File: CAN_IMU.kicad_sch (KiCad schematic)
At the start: 36 parts, among them J1 USB_C_Receptacle_USB2.0_16P, J2 TAG SWD, J3 Conn_01x05, SW1 RST, SW2 SW_DIP_x02, U1 STM32G431CBTx, U2 USBLC6-2SC6, U3 SN74LVC1G126DBV, U4 TCAN3414, U5 TPS62172DSG

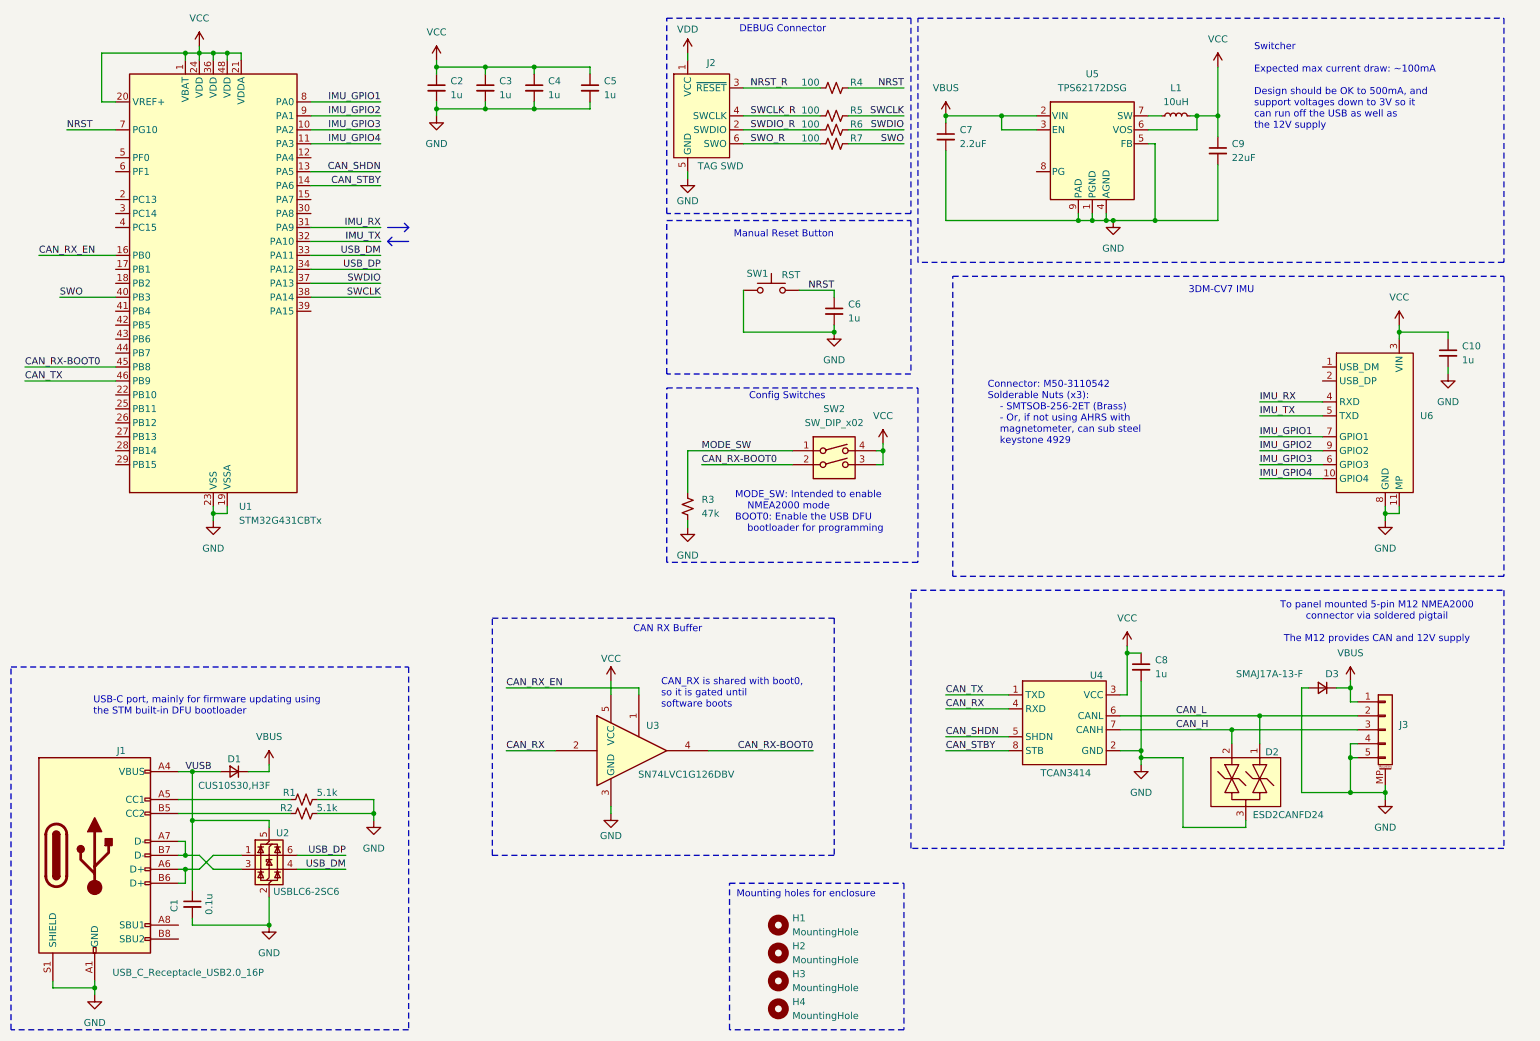
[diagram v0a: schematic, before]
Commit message: Add pulldown to CAN_RX_EN
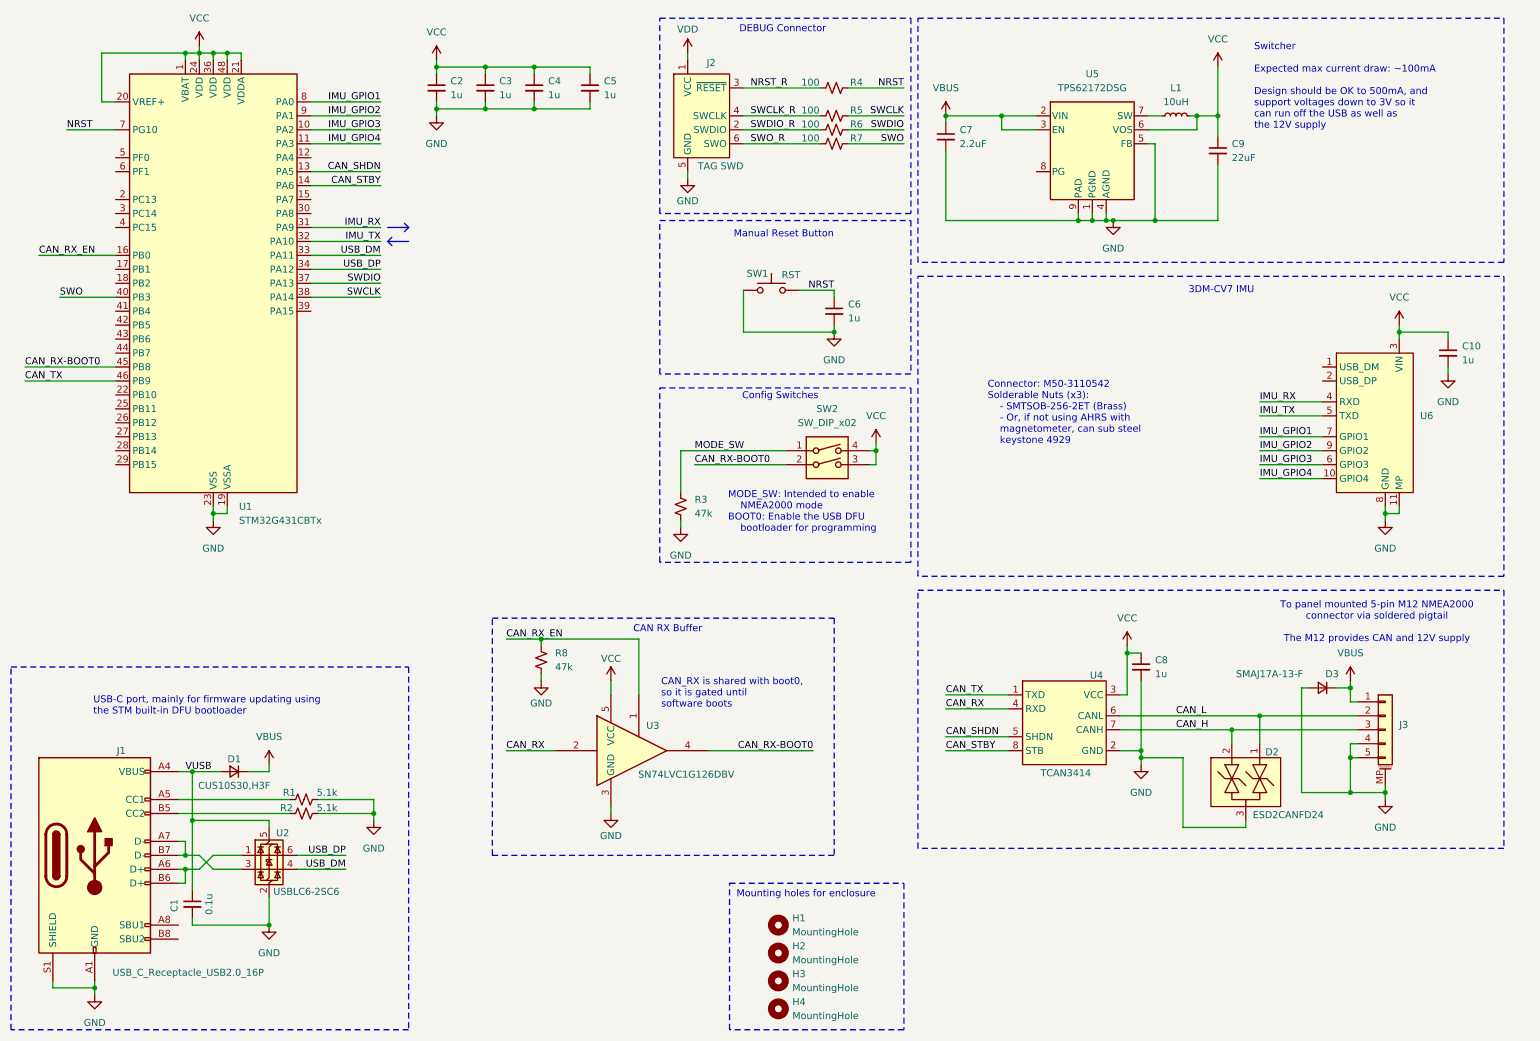
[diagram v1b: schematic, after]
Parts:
- added R8: 47k, Resistor_SMD:R_0603_1608Metric, symbol Device:R_Small_US
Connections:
- net CAN_RX_EN: now also R8.1
- net GND: now also R8.2
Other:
- moved on the sheet: R3, SW2

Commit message: Basically finished layout
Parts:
- C7: value 2.2uF -> 10uF; Digikey Part Number 1276-6702-1-ND -> 490-18663-1-ND; Mfg Part Number CL21A225KBFNNNE -> GRM21BR61H106KE43L
- L1: value 10uH -> 2.2uH; footprint Inductor_SMD:L_Bourns-SRN6028 -> RJMP_Inductors:IND_LQH5BPN2R2NT0L; Digikey Part Number 118-SRN6028C-100MCT-ND -> 490-7778-1-ND; Mfg Part Number SRN6028C-100M -> LQH5BPN2R2NT0L
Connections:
- net VDD is gone; now on net VCC: J2.1 (VCC)
- net CAN_H: now also D2.1; no longer D2.2
- net CAN_L: now also D2.2; no longer D2.1
- net CAN_RX_EN: now also U1.44 (PB7); no longer U1.16 (PB0)
- net CAN_SHDN: now also U1.41 (PB4); no longer U1.13 (PA5)
- net CAN_STBY: now also U1.43 (PB6); no longer U1.14 (PA6)
- net GND: no longer U6.11 (MP)
- net IMU_GPIO1: now also U1.28 (PB14); no longer U1.8 (PA0)
- net IMU_GPIO2: now also U1.27 (PB13); no longer U1.9 (PA1)
- net IMU_GPIO3: now also U1.25 (PB11); no longer U1.10 (PA2)
- net IMU_GPIO4: now also U1.26 (PB12); no longer U1.11 (PA3)
- net MODE_SW: now also U1.12 (PA4)
- net SW: now reaches L1.1, U5.7 (SW)
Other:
- moved on the sheet: L1

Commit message: Add part numbers and output generation
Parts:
- C10, C2, C3, C4, C5, C6, C8: LCSC Part Number (none) -> C15849
- C7: LCSC Part Number (none) -> C15850
- C9: Digikey Part Number (none) -> 1276-3047-1-ND; LCSC Part Number (none) -> C12891; Mfg Part Number (none) -> CL31A226KAHNNNE
- D1: LCSC Part Number (none) -> C146335
- D2: LCSC Part Number (none) -> C5278878
- D3: LCSC Part Number (none) -> C134963
- H1, H2, H3, H4, J2: now not fitted
- J1: LCSC Part Number (none) -> C2896636
- J3: LCSC Part Number (none) -> C265085
- L1: LCSC Part Number (none) -> C135262
- R3, R8: Digikey Part Number (none) -> 311-47.0KHRCT-ND; LCSC Part Number (none) -> C25819; Mfg Part Number (none) -> RC0603FR-0747KL
- R4, R5, R6, R7: LCSC Part Number (none) -> C105588
- SW2: LCSC Part Number (none) -> C3312524
- U1: Digikey Part Number (none) -> 497-19473-ND; LCSC Part Number (none) -> C529355; Mfg Part Number (none) -> STM32G431CBT6
- U3: LCSC Part Number (none) -> C46472327
- U4: LCSC Part Number (none) -> C22396693
- U5: Digikey Part Number (none) -> 296-39449-1-ND; LCSC Part Number (none) -> C59873; Mfg Part Number (none) -> TPS62172DSGR
- U6: Digikey Part Number (none) -> 952-2342-ND; LCSC Part Number (none) -> C6659241; Mfg Part Number (none) -> M50-3110542

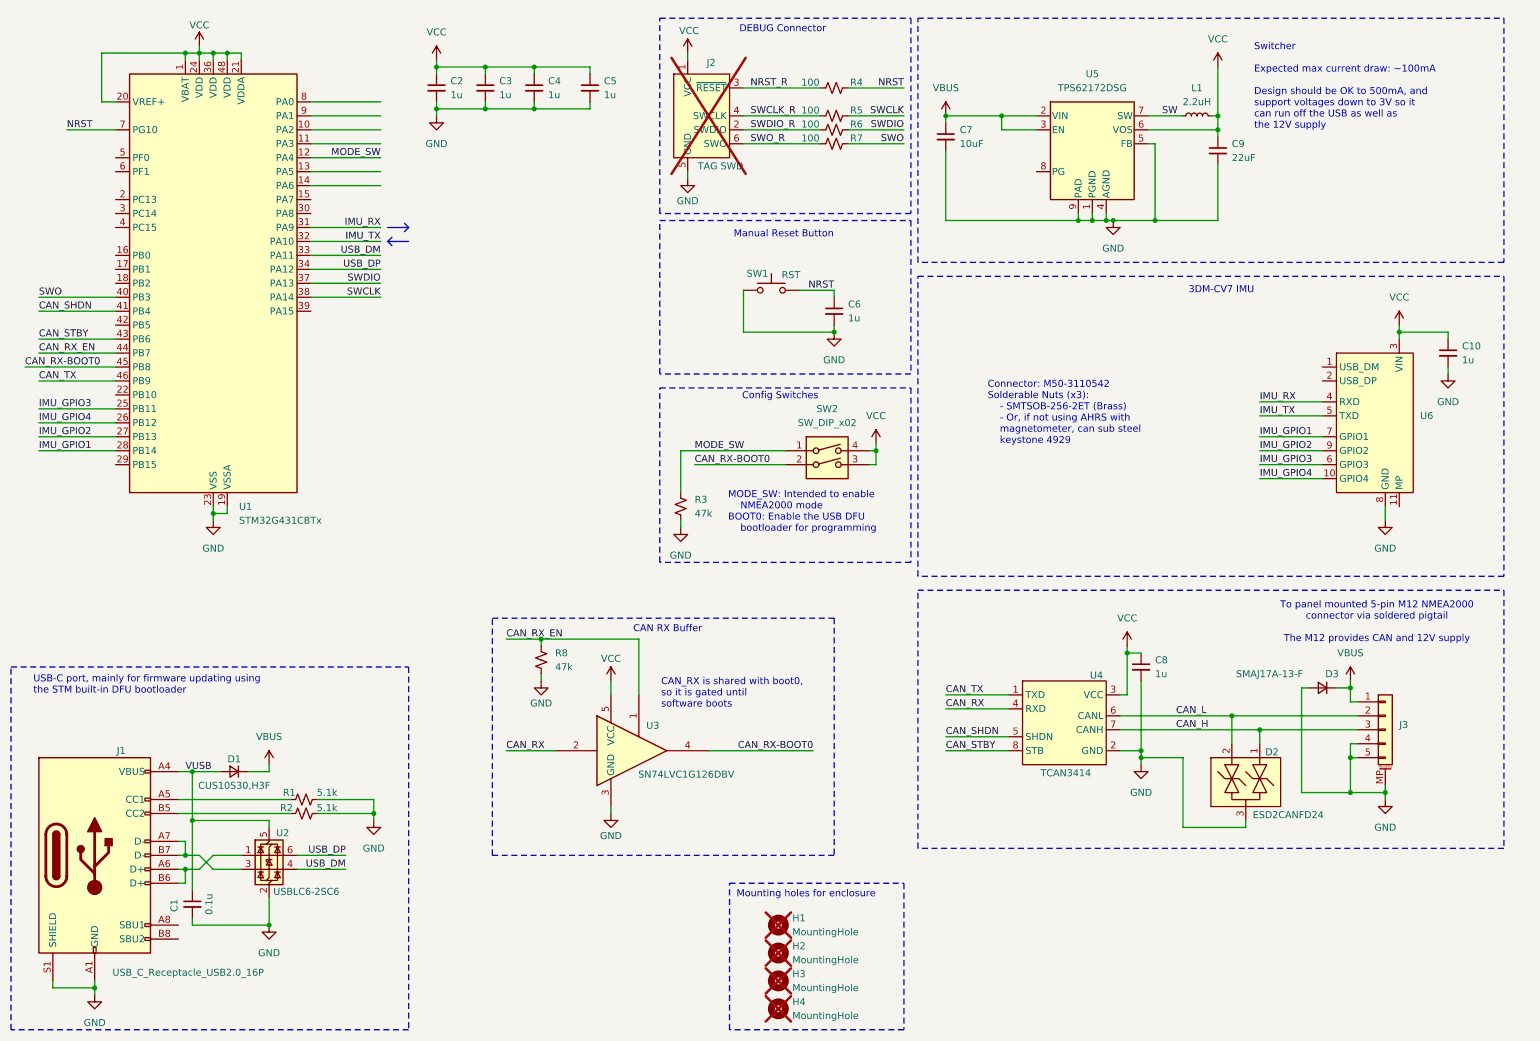
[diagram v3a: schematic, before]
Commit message: Add onboard IMU and logo
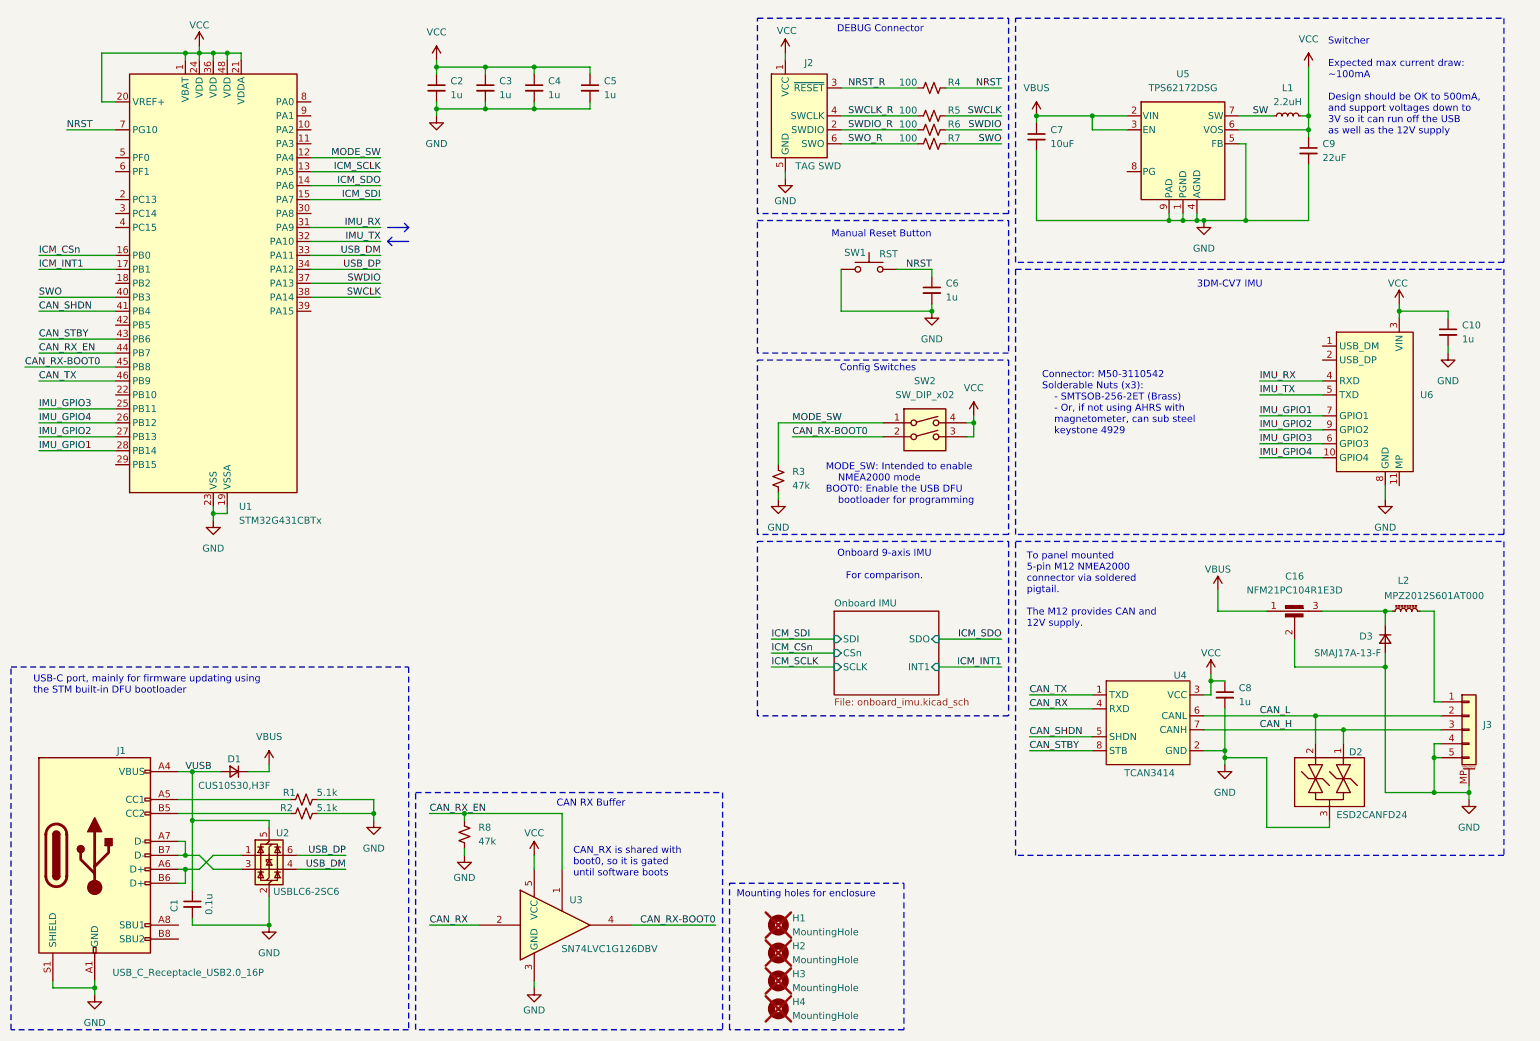
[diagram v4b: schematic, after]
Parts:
- added C16: NFM21PC104R1E3D, RJMP_Misc:NFM21PC_Feedthrough_Cap, symbol Device:C_Feedthrough
- added L2: MPZ2012S601AT000, Inductor_SMD:L_0805_2012Metric, symbol Device:L_Ferrite_Small
- J2: now fitted
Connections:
- net GND: now also C16.2
- net VBUS: now also C16.1; no longer D3.1 (K), J3.1 (Pin_1)
- net ICM_SCLK: now reaches U1.13 (PA5)
- net ICM_SDO: now reaches U1.14 (PA6)
- net ICM_SDI: now reaches U1.15 (PA7)
- net ICM_CSn: now reaches U1.16 (PB0)
- net ICM_INT1: now reaches U1.17 (PB1)
- new net: C16.3, D3.1 (K), L2.1
- new net: J3.1 (Pin_1), L2.2
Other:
- added sheet Onboard IMU (onboard_imu.kicad_sch)
- note added: "Onboard 9-axis IMU For comparison."
- note added: "To panel mounted 5-pin M12 NMEA2000 connector via soldered pigtail. The M12 provides CAN and 12V supply."
- note removed: "To panel mounted 5-pin M12 NMEA2000 connector via soldered pigtail The M12 provides CAN and 12V supply"
- moved on the sheet: C10, C6, C7, C8, C9, D2, D3, J3, L1, R3, R4, R5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

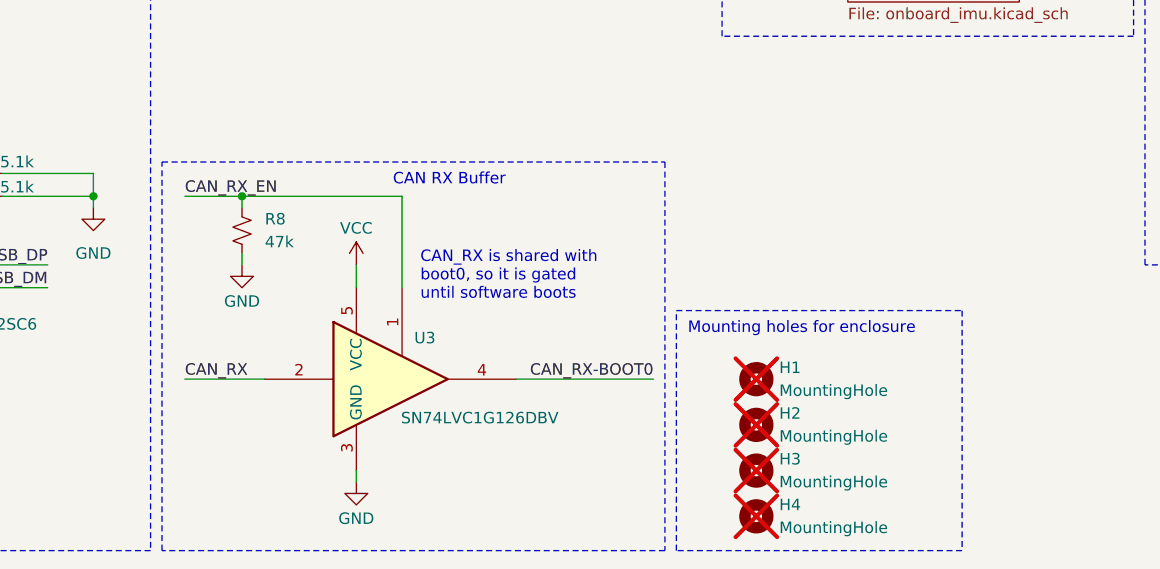
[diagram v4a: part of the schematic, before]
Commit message: Add pull-down and series resistor to CAN_RX
Prevent shorting the buffer output when throwing the DIP switch
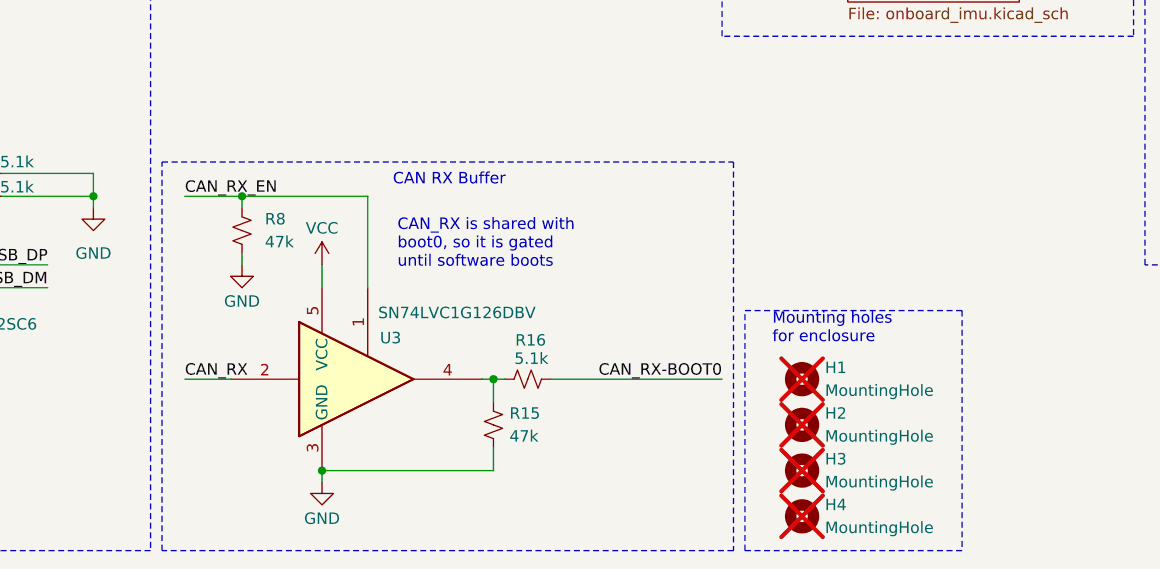
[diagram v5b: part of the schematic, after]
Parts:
- added R15: 47k, Resistor_SMD:R_0603_1608Metric, symbol Device:R_Small_US
- added R16: 5.1k, Resistor_SMD:R_0603_1608Metric, symbol Device:R_Small_US
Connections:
- net CAN_RX-BOOT0: now also R16.1; no longer U3.4
- net GND: now also R15.2
- new net: R15.1, R16.2, U3.4
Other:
- moved on the sheet: H1, H2, H3, H4, U3

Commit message: Fix some missing part numbers and update BOM
No artwork changes.
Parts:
- C16: Digikey Part Number (none) -> 490-2536-1-ND
- R4, R5, R6, R7: LCSC Part Numbe (none) -> (none)
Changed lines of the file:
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@@
-			)
-		)
-		(property "LCSC Part Numbe" " "
-			(at 180.34 30.48 0)
-			(effects
-				(font
-					(size 1.27 1.27)
-				)
-				(hide yes)
 			)
 		)
@@
 			)
 		)
+		(property "Digikey Part Number" "490-2536-1-ND"
+			(at 246.38 123.19 0)
+			(effects
+				(font
+					(size 1.27 1.27)
+				)
+				(hide yes)
+			)
+		)
 		(pin "3"
 		)
@@
 			)
 		)
-		(property "LCSC Part Numbe" " "
-			(at 180.34 25.4 0)
-			(effects
-				(font
-					(size 1.27 1.27)
-				)
-				(hide yes)
-			)
-		)
 		(property "Mfg Part Number" "RC0603FR-07100RL"
 			(at 180.34 25.4 0)
@@
 		)
 		(property "Description" "Resistor, small US symbol"
-			(at 180.34 35.56 0)
-			(effects
-				(font
-					(size 1.27 1.27)
-				)
-				(hide yes)
-			)
-		)
-		(property "LCSC Part Numbe" " "
 			(at 180.34 35.56 0)
 			(effects
@@
 			(at 180.34 33.02 0)
 			(effects
-				(font
-					(size 1.27 1.27)
-				)
-				(hide yes)
-			)
-		)
-		(property "LCSC Part Numbe" " "
-			(at 180.34 33.02 0)
-			(effects

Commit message: Rev 2 updates
- Fix microstrain connector pinout
- Update silkscreen rev
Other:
- note added: "Switcher Expected max current draw: ~100mA Design should be OK to 500mA, and support voltages down to 4.5V so it can run off the USB as well as the 12V supply"
- note removed: "Switcher Expected max current draw: ~100mA Design should be OK to 500mA, and support voltages down to 3V so it can run off the USB as well as the 12V supply"
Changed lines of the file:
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@@
 		)
 	)
-	(text "Switcher\n\nExpected max current draw: \n~100mA\n\nDesign should be OK to 500mA, \nand support voltages down to \n3V so it can run off the USB \nas well as the 12V supply"
+	(text "Switcher\n\nExpected max current draw: \n~100mA\n\nDesign should be OK to 500mA, \nand support voltages down to \n4.5V so it can run off the USB \nas well as the 12V supply"
 		(exclude_from_sim no)
 		(at 252.476 25.146 0)
@@
 		(pin "6"
 		)
-		(pin "11"
-		)
 		(pin "4"
